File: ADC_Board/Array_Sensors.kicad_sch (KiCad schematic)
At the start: 30 parts, among them IC3 INA210CQDCKRQ1, IC4 OPA990IDCKR, IC5 OPA990IDCKR, IC6 INA210CQDCKRQ1

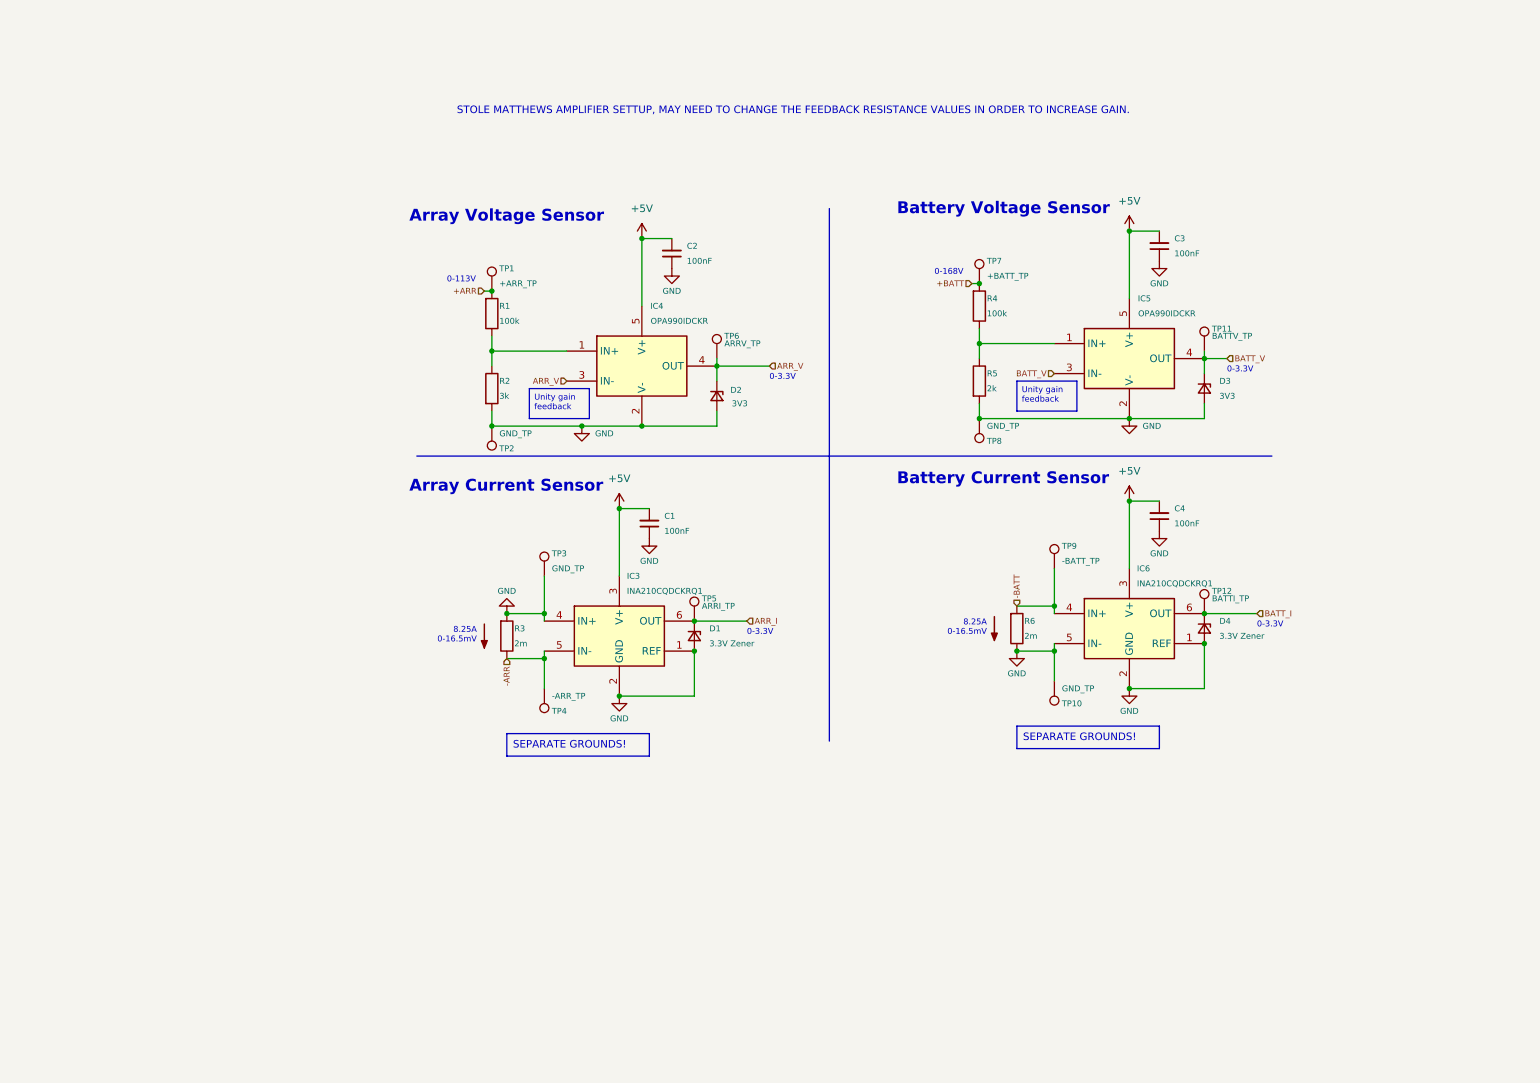
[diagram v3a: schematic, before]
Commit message: Smalll changes made to address ERC issues and review, also updated symbols and ensured all datasheets were linked
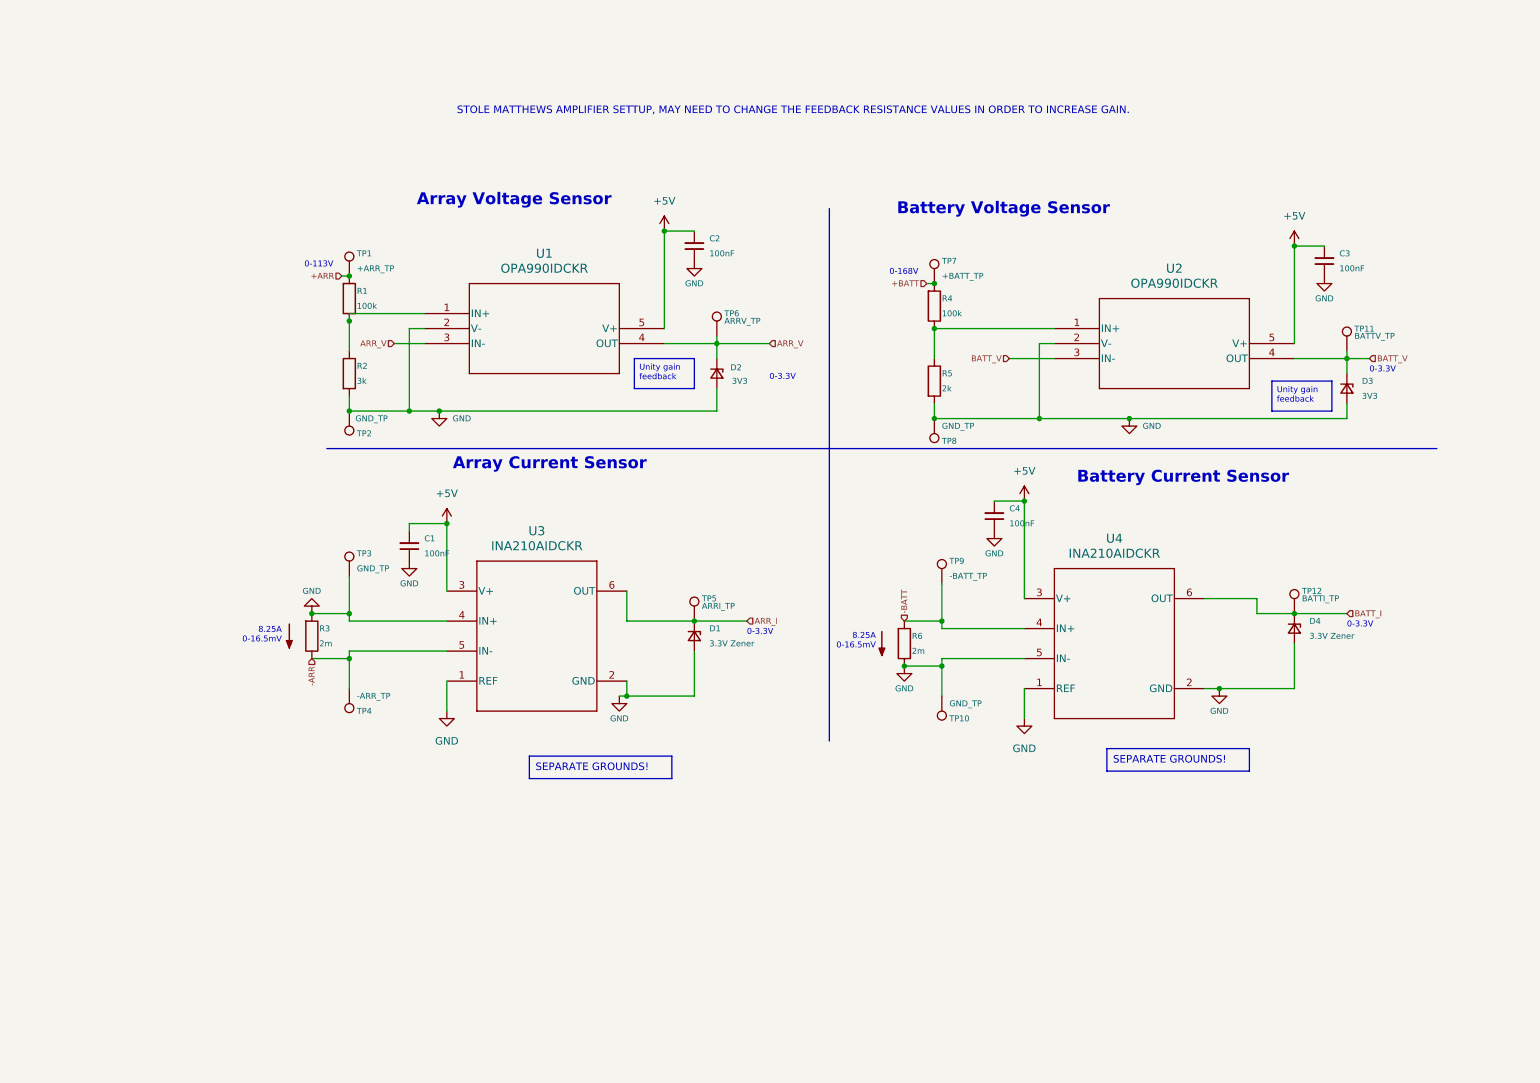
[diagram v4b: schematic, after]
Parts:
- removed IC3, IC6: INA210CQDCKRQ1, footprints:ti_INA210CQDCKRQ1, symbol ti_INA210CQDCKRQ1:INA210CQDCKRQ1
- removed IC4, IC5: OPA990IDCKR, footprints:ti_OPA990IDCKR, symbol ti_OPA990IDCKR:OPA990IDCKR
- added U1, U2: OPA990IDCKR, SC_90IDCKR_TEX, symbol OPA990:OPA990IDCKR
- added U3, U4: INA210AIDCKR, DCK0006A_N, symbol INA210:INA210AIDCKR
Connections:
- net +5V: now also U1.5 (V+), U2.5 (V+), U3.3 (V+), U4.3 (V+)
- net -ARR: now also U3.5 (IN-)
- net -BATT: now also U4.4 (IN+)
- net ARR_I: now also U3.6 (OUT)
- net ARR_V: now also U1.3 (IN-), U1.4 (OUT)
- net BATT_I: now also U4.6 (OUT)
- net BATT_V: now also U2.3 (IN-), U2.4 (OUT)
- net GND: now also U1.2 (V-), U2.2 (V-), U3.1 (REF), U3.2 (GND), U3.4 (IN+), U4.1 (REF), U4.2 (GND), U4.5 (IN-)
- net at R4.1, R5.1: now also U2.1 (IN+)
- net at R1.1, R2.1: now also U1.1 (IN+)
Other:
- moved on the sheet: C1, C2, C3, C4, D2, D3, D4, R1, R2, R3, R4, R5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

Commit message: Created Layout
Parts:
- C1, C2, C3, C4: footprint Capacitor_SMD:C_0402_1005Metric -> Capacitor_SMD:C_0805_2012Metric
- D1, D2, D3, D4: footprint Diode_SMD:D_MiniMELF -> Diode_SMD:D_0805_2012Metric
- R3, R6: footprint Resistor_SMD:R_1206_3216Metric -> Resistor_THT:R_Axial_Power_L20.0mm_W6.4mm_P30.48mm
- TP1, TP10, TP11, TP12, TP2, TP3, TP4, TP5, TP6, TP7, TP8, TP9: footprint TestPoint:TestPoint_Pad_1.0x1.0mm -> UTSVT_Special:TestPoint_HEX_3mmID
- U1, U2: footprint SC_90IDCKR_TEX -> OPA990:SC_90IDCKR_TEX
- U3, U4: footprint DCK0006A_N -> INA210:DCK0006A_N
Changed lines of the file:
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@@
 			)
 		)
-		(property "Footprint" "Diode_SMD:D_MiniMELF"
+		(property "Footprint" "Diode_SMD:D_0805_2012Metric"
 			(at 133.35 120.65 90)
 			(effects
@@
 			)
 		)
-		(property "Footprint" "DCK0006A_N"
+		(property "Footprint" "INA210:DCK0006A_N"
 			(at 106.68 120.65 0)
 			(effects
@@
 			)
 		)
-		(property "Footprint" "Capacitor_SMD:C_0402_1005Metric"
+		(property "Footprint" "Capacitor_SMD:C_0805_2012Metric"
 			(at 124.46 55.88 0)
 			(effects
@@
 			)
 		)
-		(property "Footprint" "Capacitor_SMD:C_0402_1005Metric"
+		(property "Footprint" "Capacitor_SMD:C_0805_2012Metric"
 			(at 231.14 58.42 0)
 			(effects
@@
 			)
 		)
-		(property "Footprint" "TestPoint:TestPoint_Pad_1.0x1.0mm"
+		(property "Footprint" "UTSVT_Special:TestPoint_HEX_3mmID"
 			(at 74.93 82.55 0)
 			(effects
@@
 			)
 		)
-		(property "Footprint" "Capacitor_SMD:C_0402_1005Metric"
+		(property "Footprint" "Capacitor_SMD:C_0805_2012Metric"
 			(at 175.26 101.6 0)
 			(effects
@@
 			)
 		)
-		(property "Footprint" "TestPoint:TestPoint_Pad_1.0x1.0mm"
+		(property "Footprint" "UTSVT_Special:TestPoint_HEX_3mmID"
 			(at 74.93 129.54 0)
 			(effects
@@
 			)
 		)
-		(property "Footprint" "DCK0006A_N"
+		(property "Footprint" "INA210:DCK0006A_N"
 			(at 204.47 121.92 0)
 			(effects
@@
 			)
 		)
-		(property "Footprint" "TestPoint:TestPoint_Pad_1.0x1.0mm"
+		(property "Footprint" "UTSVT_Special:TestPoint_HEX_3mmID"
 			(at 175.26 111.76 0)
 			(effects
@@
 			)
 		)
-		(property "Footprint" "TestPoint:TestPoint_Pad_1.0x1.0mm"
+		(property "Footprint" "UTSVT_Special:TestPoint_HEX_3mmID"
 			(at 137.16 69.85 0)
 			(effects
@@
 			)
 		)
-		(property "Footprint" "Diode_SMD:D_MiniMELF"
+		(property "Footprint" "Diode_SMD:D_0805_2012Metric"
 			(at 234.95 119.38 90)
 			(effects
@@
 			)
 		)
-		(property "Footprint" "TestPoint:TestPoint_Pad_1.0x1.0mm"
+		(property "Footprint" "UTSVT_Special:TestPoint_HEX_3mmID"
 			(at 74.93 59.69 0)
 			(effects
@@
 			)
 		)
-		(property "Footprint" "TestPoint:TestPoint_Pad_1.0x1.0mm"
+		(property "Footprint" "UTSVT_Special:TestPoint_HEX_3mmID"
 			(at 138.43 118.11 0)
 			(effects
@@
 			)
 		)
-		(property "Footprint" "SC_90IDCKR_TEX"
+		(property "Footprint" "OPA990:SC_90IDCKR_TEX"
 			(at 194.31 68.58 0)
 			(effects
@@
 			)
 		)
-		(property "Footprint" "Resistor_SMD:R_1206_3216Metric"
+		(property "Footprint" "Resistor_THT:R_Axial_Power_L20.0mm_W6.4mm_P30.48mm"
 			(at 167.132 121.92 90)
 			(effects
@@
 			)
 		)
-		(property "Footprint" "Capacitor_SMD:C_0402_1005Metric"
+		(property "Footprint" "Capacitor_SMD:C_0805_2012Metric"
 			(at 76.2 106.68 0)
 			(effects
@@
 			)
 		)
-		(property "Footprint" "Diode_SMD:D_MiniMELF"
+		(property "Footprint" "Diode_SMD:D_0805_2012Metric"
 			(at 137.16 76.2 90)
 			(effects
@@
 			)
 		)
-		(property "Footprint" "SC_90IDCKR_TEX"
+		(property "Footprint" "OPA990:SC_90IDCKR_TEX"
 			(at 87.63 66.04 0)
 			(effects
@@
 			)
 		)
-		(property "Footprint" "Diode_SMD:D_MiniMELF"
+		(property "Footprint" "Diode_SMD:D_0805_2012Metric"
 			(at 243.84 78.74 90)
 			(effects
@@
 			)
 		)
-		(property "Footprint" "TestPoint:TestPoint_Pad_1.0x1.0mm"
+		(property "Footprint" "UTSVT_Special:TestPoint_HEX_3mmID"
 			(at 243.84 72.39 0)
 			(effects
@@
 			)
 		)
-		(property "Footprint" "TestPoint:TestPoint_Pad_1.0x1.0mm"
+		(property "Footprint" "UTSVT_Special:TestPoint_HEX_3mmID"
 			(at 74.93 110.49 0)
 			(effects
@@
 			)
 		)
-		(property "Footprint" "TestPoint:TestPoint_Pad_1.0x1.0mm"
+		(property "Footprint" "UTSVT_Special:TestPoint_HEX_3mmID"
 			(at 175.26 130.81 0)
 			(effects
@@
 			)
 		)
-		(property "Footprint" "Resistor_SMD:R_1206_3216Metric"
+		(property "Footprint" "Resistor_THT:R_Axial_Power_L20.0mm_W6.4mm_P30.48mm"
 			(at 66.802 120.65 90)
 			(effects
@@
 			)
 		)
-		(property "Footprint" "TestPoint:TestPoint_Pad_1.0x1.0mm"
+		(property "Footprint" "UTSVT_Special:TestPoint_HEX_3mmID"
 			(at 173.99 83.82 0)
 			(effects
@@
 			)
 		)
-		(property "Footprint" "TestPoint:TestPoint_Pad_1.0x1.0mm"
+		(property "Footprint" "UTSVT_Special:TestPoint_HEX_3mmID"
 			(at 240.03 116.84 0)
 			(effects
@@
 			)
 		)
-		(property "Footprint" "TestPoint:TestPoint_Pad_1.0x1.0mm"
+		(property "Footprint" "UTSVT_Special:TestPoint_HEX_3mmID"
 			(at 173.99 60.96 0)
 			(effects

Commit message: Added a few small things to address reviews. Made a lot of improvements to readability.
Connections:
- net -BATT: now also R6.1, TP10.1, U4.5 (IN-); no longer R6.2, TP9.1, U4.4 (IN+)
- net GND: now also R6.2, TP9.1, U4.4 (IN+); no longer R6.1, TP10.1, U4.5 (IN-)
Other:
- note added: "0-135V"
- note removed: "0-168V"
- note removed: "8.25A 0-16.5mV"
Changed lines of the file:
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@@
 	(paper "A4")
 	(junction
-		(at 168.91 125.73)
-		(diameter 0)
-		(color 0 0 0 0)
-	)
-	(junction
 		(at 74.93 82.55)
 		(diameter 0)
@@
 	)
 	(junction
+		(at 168.91 118.11)
+		(diameter 0)
+		(color 0 0 0 0)
+	)
+	(junction
+		(at 68.58 116.84)
+		(diameter 0)
+		(color 0 0 0 0)
+	)
+	(junction
 		(at 121.92 130.81)
 		(diameter 0)
@@
 	)
 	(junction
-		(at 68.58 116.84)
-		(diameter 0)
-		(color 0 0 0 0)
-	)
-	(junction
 		(at 173.99 83.82)
 		(diameter 0)
@@
 		)
 	)
-	(text_box "SEPARATE GROUNDS!"
-		(exclude_from_sim no)
-		(at 105.41 140.97 0)
-		(size 24.13 3.81)
-		(stroke
-			(width 0)
-			(type default)
-		)
-		(fill
-			(type none)
-		)
-		(effects
-			(font
-				(size 1.27 1.27)
-			)
-			(justify left top)
-		)
-	)
 	(text_box "Unity gain feedback"
 		(exclude_from_sim no)
@@
 		)
 	)
-	(text_box "SEPARATE GROUNDS!"
-		(exclude_from_sim no)
-		(at 203.2 139.7 0)
-		(size 24.13 3.81)
-		(stroke
-			(width 0)
-			(type default)
-		)
-		(fill
-			(type none)
-		)
-		(effects
-			(font
-				(size 1.27 1.27)
-			)
-			(justify left top)
-		)
-	)
-	(text "8.25A\n0-16.5mV"
-		(exclude_from_sim no)
-		(at 164.084 122.936 0)
-		(effects
-			(font
-				(size 1 1)
-			)
-			(justify right bottom)
-		)
-	)
 	(text "0-3.3V"
 		(exclude_from_sim no)
@@
 		)
 	)
-	(text "8.25A\n0-16.5mV"
-		(exclude_from_sim no)
-		(at 63.5 121.92 0)
-		(effects
-			(font
-				(size 1 1)
-			)
-			(justify right bottom)
-		)
-	)
 	(text "Battery Current Sensor"
 		(exclude_from_sim no)
@@
 		)
 	)
-	(text "0-168V"
+	(text "0-135V"
 		(exclude_from_sim no)
 		(at 166.37 59.69 0)
@@
 		)
 	)
-	(hierarchical_label "BATT_V"
+	(hierarchical_label "-BATT"
 		(shape input)
-		(at 186.69 73.66 180)
+		(at 168.91 125.73 270)
 		(fields_autoplaced yes)
 		(effects
@@
 	(hierarchical_label "BATT_V"
 		(shape input)
-		(at 247.65 73.66 0)
+		(at 186.69 73.66 180)
 		(fields_autoplaced yes)
 		(effects
@@
 				(size 1 1)
 			)
-			(justify left)
+			(justify right)
 		)
 	)
-	(hierarchical_label "+BATT"
+	(hierarchical_label "BATT_V"
 		(shape input)
-		(at 172.72 60.96 180)
+		(at 247.65 73.66 0)
 		(fields_autoplaced yes)
 		(effects
@@
 				(size 1 1)
 			)
-			(justify right)
+			(justify left)
 		)
 	)
-	(hierarchical_label "-BATT"
+	(hierarchical_label "+BATT"
 		(shape input)
-		(at 168.91 118.11 90)
+		(at 172.72 60.96 180)
 		(fields_autoplaced yes)
 		(effects
@@
 				(size 1 1)
 			)
-			(justify left)
+			(justify right)
 		)
 	)
@@
 		)
 	)
-	(hierarchical_label "-ARR"
+	(hierarchical_label "BATT_I"
 		(shape input)
-		(at 68.58 124.46 270)
+		(at 243.84 116.84 0)
 		(fields_autoplaced yes)
 		(effects
@@
 				(size 1 1)
 			)
-			(justify right)
+			(justify left)
 		)
 	)
-	(hierarchical_label "BATT_I"
+	(hierarchical_label "ARR_V"
 		(shape input)
-		(at 243.84 116.84 0)
+		(at 82.55 71.12 180)
 		(fields_autoplaced yes)
 		(effects
@@
 				(size 1 1)
 			)
-			(justify left)
+			(justify right)
 		)
 	)
-	(hierarchical_label "ARR_V"
+	(hierarchical_label "-ARR"
 		(shape input)
-		(at 82.55 71.12 180)
+		(at 68.58 124.46 270)
 		(fields_autoplaced yes)
 		(effects
@@
 	(symbol
 		(lib_id "power:GND")
-		(at 168.91 125.73 0)
-		(unit 1)
-		(exclude_from_sim no)
-		(in_bom yes)
-		(on_board yes)
-		(dnp no)
-		(property "Reference" "#PWR027"
-			(at 168.91 132.08 0)
-			(effects
-				(font
-					(size 1 1)
-				)
-				(hide yes)
-			)
-		)
-		(property "Value" "GND"
-			(at 168.91 129.54 0)
-			(effects
-				(font
-					(size 1 1)
-				)
-			)
-		)
-		(property "Footprint" ""
-			(at 168.91 125.73 0)
-			(effects
-				(font
-					(size 1 1)
-				)
-				(hide yes)
-			)
-		)
-		(property "Datasheet" ""
-			(at 168.91 125.73 0)
-			(effects
-				(font
-					(size 1 1)
-				)
-				(hide yes)
-			)
-		)
-		(property "Description" "Power symbol creates a global label with name \"GND\" , ground"
-			(at 168.91 125.73 0)
-			(effects
-				(font
-					(size 1.27 1.27)
-				)
-				(hide yes)
-			)
-		)
-		(pin "1"
-		)
-		(instances
-			(project "ADC_Board"
-				(path "/c2f67899-b13b-465e-9c4c-85240262cdf4/165319c5-7975-442a-9dd1-2afd76ad42a5"
-					(reference "#PWR027")
-					(unit 1)
-				)
-			)
-		)
-	)
-	(symbol
-		(lib_id "power:GND")
 		(at 85.09 107.95 0)
 		(unit 1)
@@
 	)
 	(symbol
+		(lib_id "power:GND")
+		(at 168.91 118.11 180)
+		(unit 1)
+		(exclude_from_sim no)
+		(in_bom yes)
+		(on_board yes)
+		(dnp no)
+		(property "Reference" "#PWR027"
+			(at 168.91 111.76 0)
+			(effects
+				(font
+					(size 1 1)
+				)
+				(hide yes)
+			)
+		)
+		(property "Value" "GND"
+			(at 168.91 114.3 0)
+			(effects
+				(font
+					(size 1 1)
+				)
+			)
+		)
+		(property "Footprint" ""
+			(at 168.91 118.11 0)
+			(effects
+				(font
+					(size 1 1)
+				)
+				(hide yes)
+			)
+		)
+		(property "Datasheet" ""
+			(at 168.91 118.11 0)
+			(effects
+				(font
+					(size 1 1)
+				)
+				(hide yes)
+			)
+		)
+		(property "Description" "Power symbol creates a global label with name \"GND\" , ground"
+			(at 168.91 118.11 0)
+			(effects
+				(font
+					(size 1.27 1.27)
+				)
+				(hide yes)
+			)
+		)
+		(pin "1"
+		)
+		(instances
+			(project "ADC_Board"
+				(path "/c2f67899-b13b-465e-9c4c-85240262cdf4/165319c5-7975-442a-9dd1-2afd76ad42a5"
+					(reference "#PWR027")
+					(unit 1)
+				)
+			)
+		)
+	)
+	(symbol
 		(lib_id "Device:R")
 		(at 74.93 63.5 0)
@@
 	)
 	(symbol
-		(lib_id "power:GND")
-		(at 68.58 116.84 180)
-		(unit 1)
-		(exclude_from_sim no)
-		(in_bom yes)
-		(on_board yes)
-		(dnp no)
-		(fields_autoplaced yes)
-		(property "Reference" "#PWR09"
-			(at 68.58 110.49 0)
-			(effects
-				(font
-					(size 1 1)
-				)
-				(hide yes)
-			)
-		)
-		(property "Value" "GND"
-			(at 68.58 113.03 0)
-			(effects
-				(font
-					(size 1 1)
-				)
-			)
-		)
-		(property "Footprint" ""
-			(at 68.58 116.84 0)
-			(effects
-				(font
-					(size 1 1)
-				)
-				(hide yes)
-			)
-		)
-		(property "Datasheet" ""
-			(at 68.58 116.84 0)
-			(effects
-				(font
-					(size 1 1)
-				)
-				(hide yes)
-			)
-		)
-		(property "Description" "Power symbol creates a global label with name \"GND\" , ground"
-			(at 68.58 116.84 0)
-			(effects
-				(font
-					(size 1.27 1.27)
-				)
-				(hide yes)
-			)
-		)
-		(pin "1"
-		)
-		(instances
-			(project "ADC_Board"
-				(path "/c2f67899-b13b-465e-9c4c-85240262cdf4/165319c5-7975-442a-9dd1-2afd76ad42a5"
-					(reference "#PWR09")
-					(unit 1)
-				)
-			)
-		)
-	)
-	(symbol
 		(lib_id "Connector:TestPoint")
 		(at 74.93 129.54 0)
@@
 					(unit 1)
 				)
+			)
+		)
+	)
+	(symbol
+		(lib_id "power:GND")
+		(at 68.58 116.84 180)
+		(unit 1)
+		(exclude_from_sim no)
+		(in_bom yes)
+		(on_board yes)
+		(dnp no)
+		(fields_autoplaced yes)
+		(property "Reference" "#PWR09"
+			(at 68.58 110.49 0)
+			(effects
+				(font
+					(size 1 1)
+				)
+				(hide yes)
+			)
+		)
+		(property "Value" "GND"
+			(at 68.58 111.76 0)
+			(effects
+				(font
+					(size 1 1)
+				)
+			)
+		)
+		(property "Footprint" ""
+			(at 68.58 116.84 0)
+			(effects
+				(font
+					(size 1 1)
+				)
+				(hide yes)
+			)
+		)
+		(property "Datasheet" ""
+			(at 68.58 116.84 0)
+			(effects
+				(font
+					(size 1 1)
+				)
+				(hide yes)
+			)
+		)
+		(property "Description" "Power symbol creates a global label with name \"GND\" , ground"
+			(at 68.58 116.84 0)
+			(effects
+				(font
+					(size 1.27 1.27)
+				)
+				(hide yes)
+			)
+		)
+		(pin "1"
+		)
+		(instances
+			(project "ADC_Board"
+				(path "/c2f67899-b13b-465e-9c4c-85240262cdf4/165319c5-7975-442a-9dd1-2afd76ad42a5"
+					(reference "#PWR09")
+					(unit 1)
+				)
